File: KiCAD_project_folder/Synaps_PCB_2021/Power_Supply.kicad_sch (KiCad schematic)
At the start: 35 parts, among them J1 USB_C_Receptacle, Q2 Q_PMOS_DGS, U1 MAX14748BEWW+

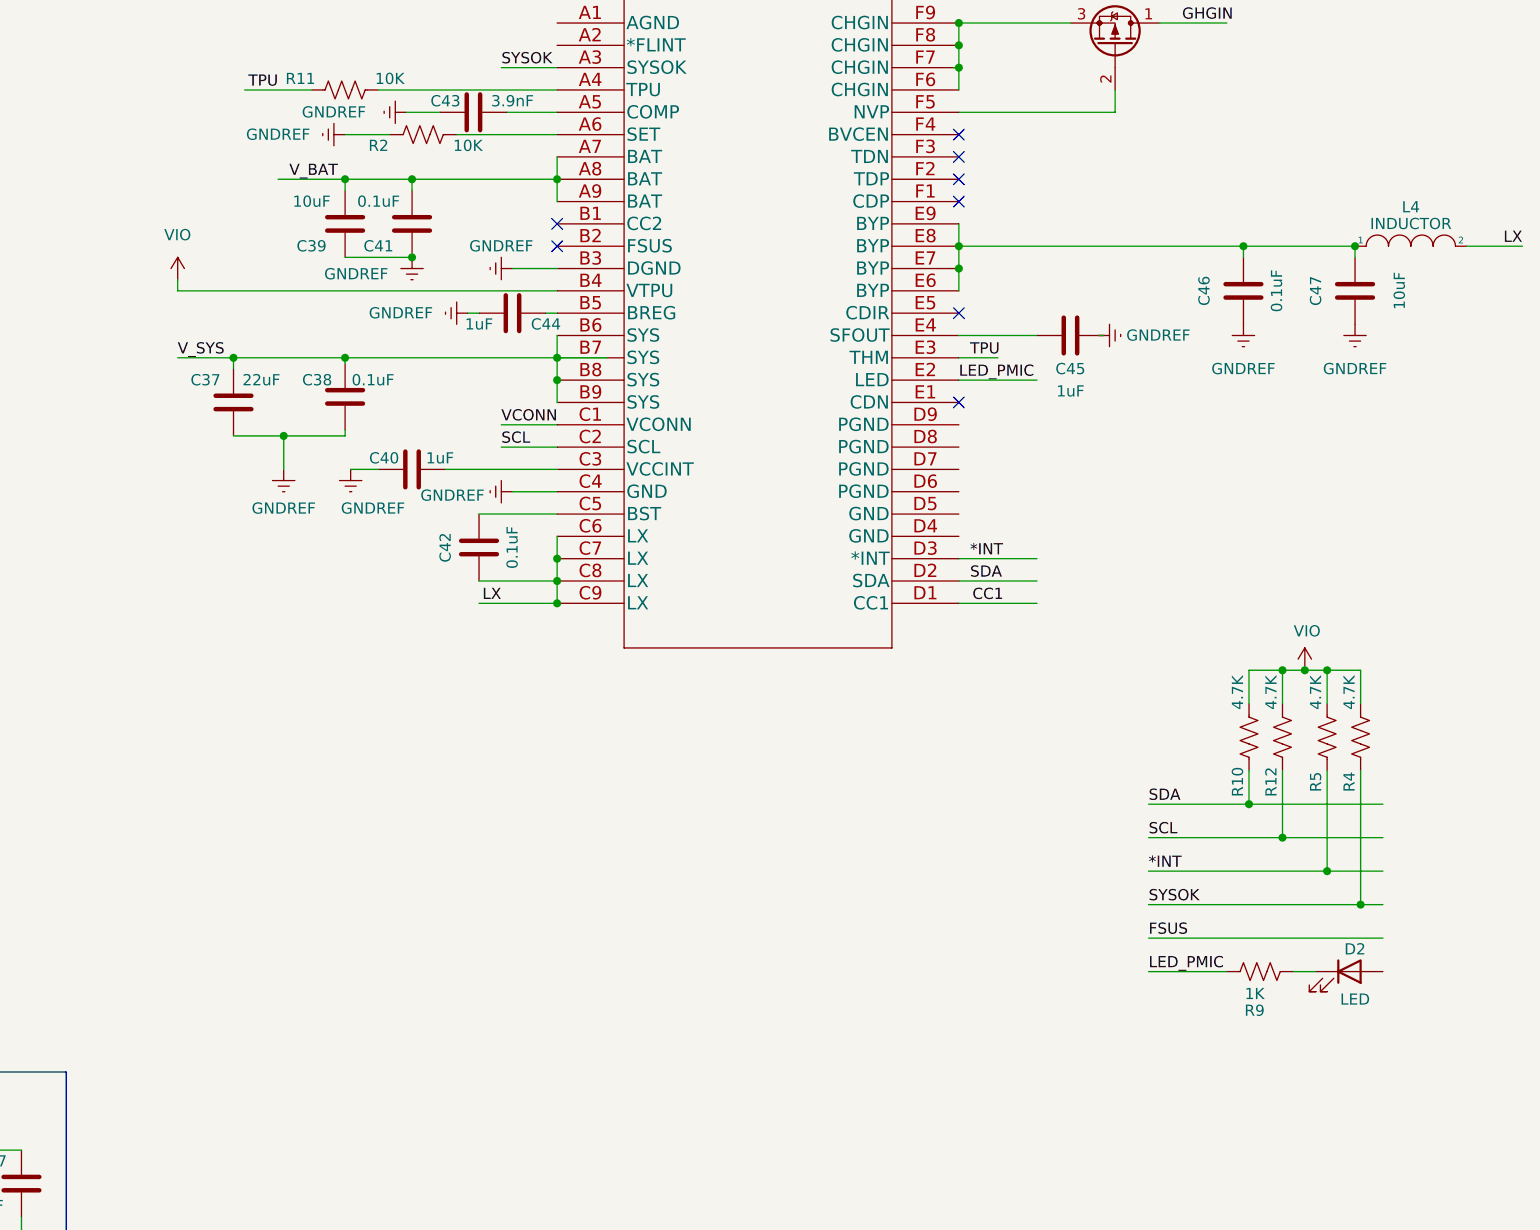
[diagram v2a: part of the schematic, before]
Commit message: Reworded PMIC and probe select
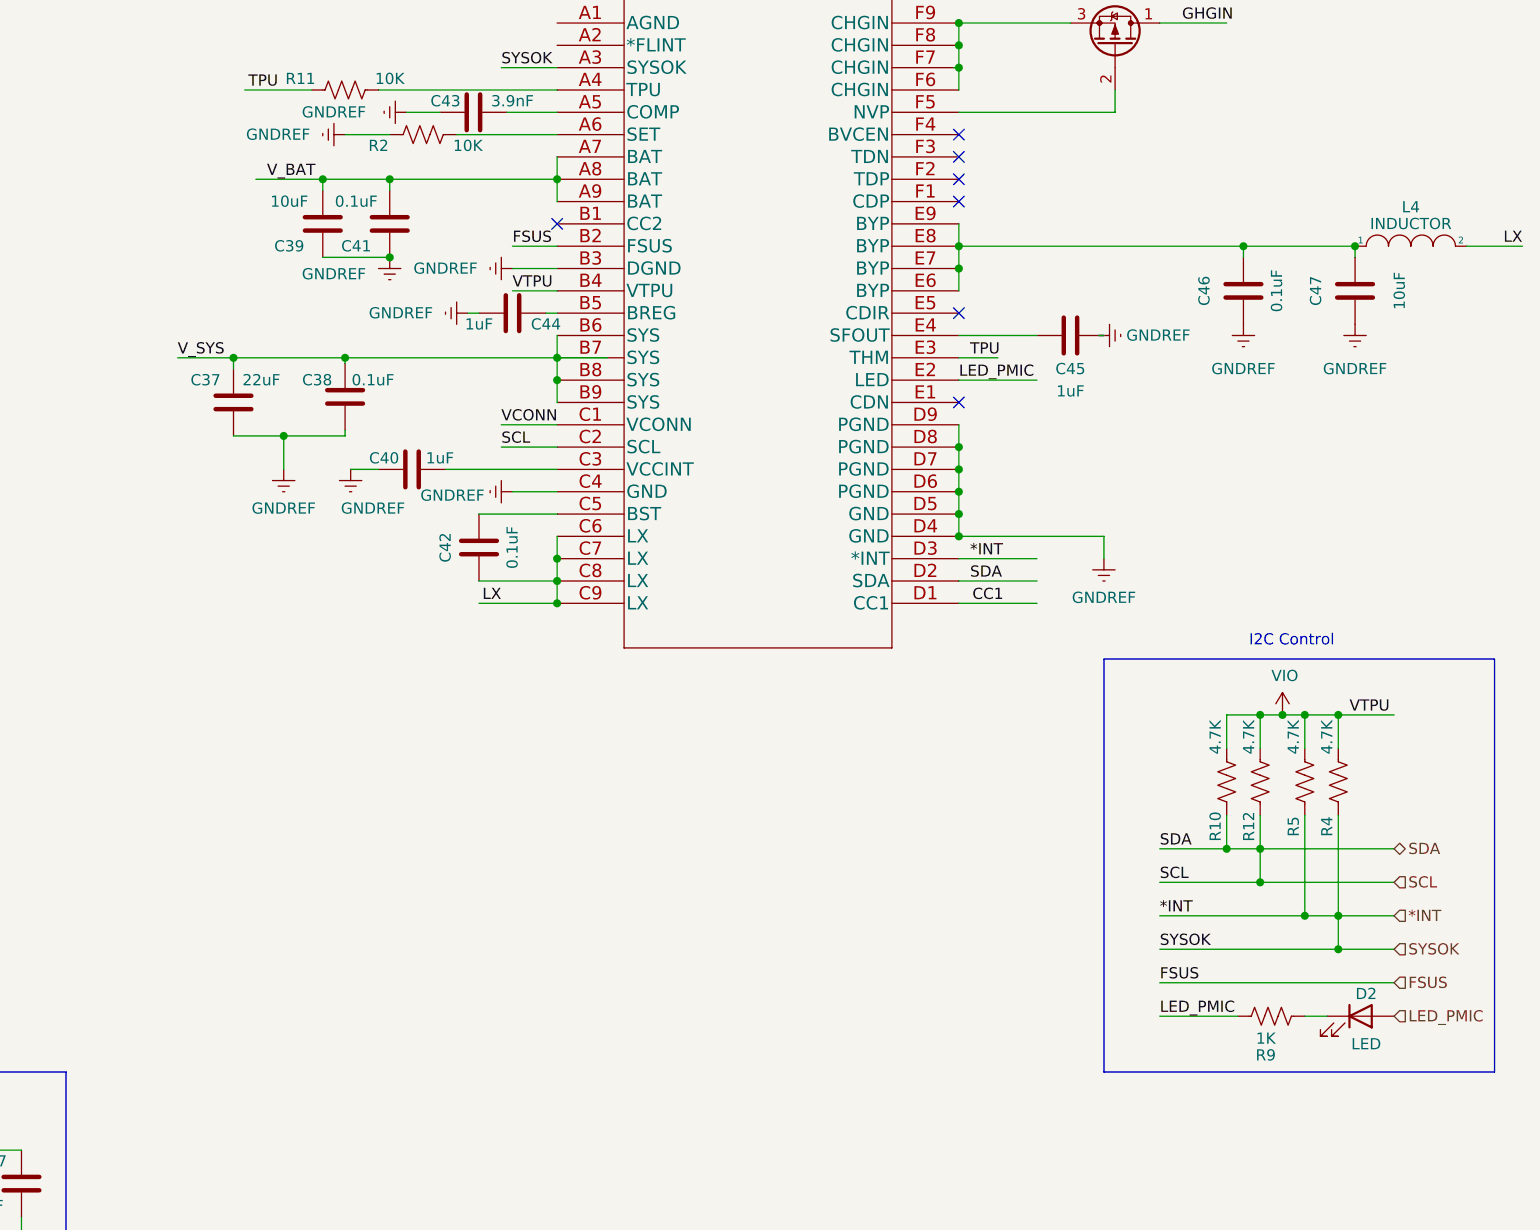
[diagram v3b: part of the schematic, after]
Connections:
- net SDA is gone; now on net SCL: R10.2, U1.D2 (SDA)
- net SYSOK is gone; now on net *INT: R4.1, U1.A3 (SYSOK)
- net FSUS: now also U1.B2 (FSUS)
- net GNDREF: now also U1.D4 (GND), U1.D5 (GND), U1.D6 (PGND), U1.D7 (PGND), U1.D8 (PGND), U1.D9 (PGND)
- net LED_PMIC: now also D2.2 (A)
- no-connect marks 16 -> 15
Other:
- note added: "I2C Control"
- moved on the sheet: C39, C41, D2, R10, R12, R4, R5, R9

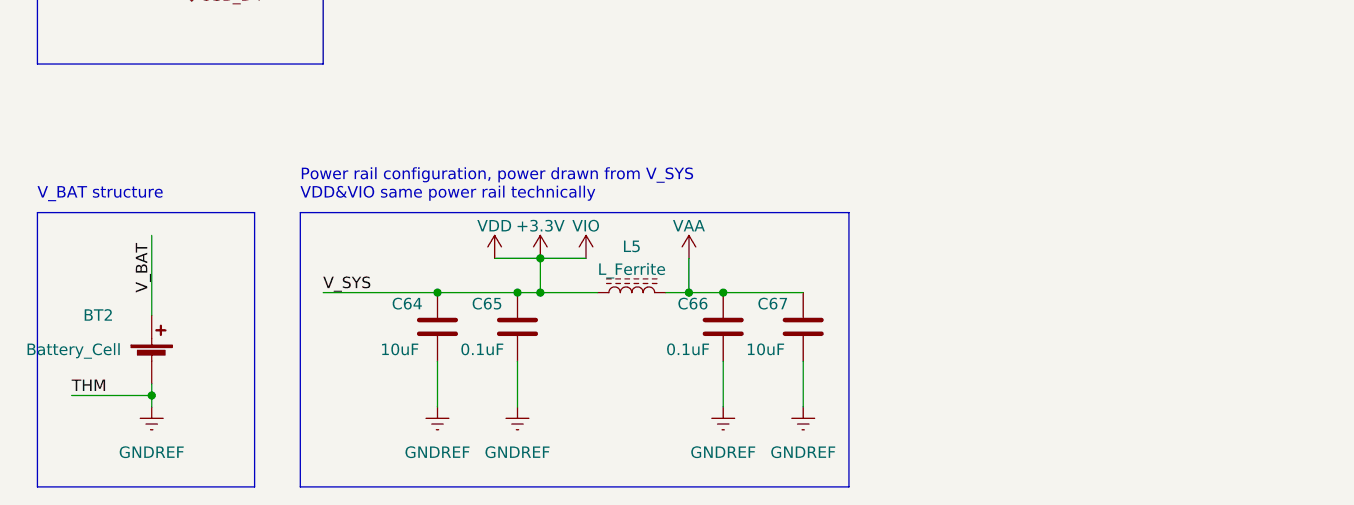
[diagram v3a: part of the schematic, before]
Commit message: Redid schematic, fixed wrong setup
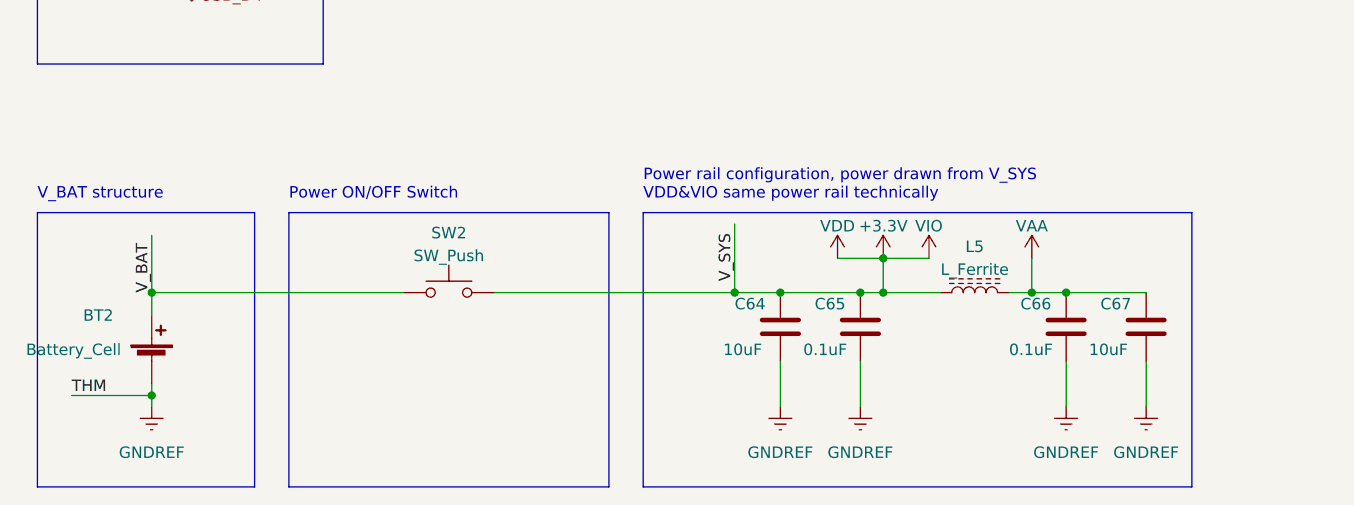
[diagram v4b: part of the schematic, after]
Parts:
- added SW2: SW_Push, symbol Switch:SW_Push
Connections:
- net +1V1: now also SW2.2
- net V_BAT: now also SW2.1
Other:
- note added: "Power ON/OFF Switch"
- moved on the sheet: C64, C65, C66, C67, L5

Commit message: Updated pcb editor with the new components imported
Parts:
- C64, C65, C66, C67: footprint (none) -> Capacitor_SMD:C_1206_3216Metric_Pad1.33x1.80mm_HandSolder
- L5: footprint (none) -> Ferrite_THT:LairdTech_28C0236-0JW-10
- Q2: footprint (none) -> Transformer_NF_ETAL_P2781
- R3: footprint (none) -> Resistor_SMD:R_1206_3216Metric_Pad1.30x1.75mm_HandSolder
- SW2: footprint (none) -> Button_Switch_SMD:SW_Push_1P1T_NO_6x6mm_H9.5mm
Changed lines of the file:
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@@
       (effects (font (size 1.27 1.27)) (justify right))
     )
-    (property "Footprint" "" (id 2) (at 27.686 101.346 90)
+    (property "Footprint" "Resistor_SMD:R_1206_3216Metric_Pad1.30x1.75mm_HandSolder" (id 2) (at 27.686 101.346 90)
       (effects (font (size 1.27 1.27)) hide)
     )
@@
     (property "Reference" "Q2" (id 0) (at 228.6 36.195 90))
     (property "Value" "Q_PMOS_DGS" (id 1) (at 228.6 38.735 90))
-    (property "Footprint" "" (id 2) (at 231.14 40.64 0)
+    (property "Footprint" "Transformer_NF_ETAL_P2781" (id 2) (at 231.14 40.64 0)
       (effects (font (size 1.27 1.27)) hide)
     )
@@
     (property "Reference" "L5" (id 0) (at 123.19 166.3532 90))
     (property "Value" "L_Ferrite" (id 1) (at 123.19 168.8901 90))
-    (property "Footprint" "" (id 2) (at 123.19 171.45 0)
+    (property "Footprint" "Ferrite_THT:LairdTech_28C0236-0JW-10" (id 2) (at 123.19 171.45 0)
       (effects (font (size 1.27 1.27)) hide)
     )
@@
       (effects (font (size 1.27 1.27)) (justify left))
     )
-    (property "Footprint" "" (id 2) (at 134.3152 179.07 0)
+    (property "Footprint" "Capacitor_SMD:C_1206_3216Metric_Pad1.33x1.80mm_HandSolder" (id 2) (at 134.3152 179.07 0)
       (effects (font (size 1.27 1.27)) hide)
     )
@@
       (effects (font (size 1.27 1.27)) (justify left))
     )
-    (property "Footprint" "" (id 2) (at 143.2052 179.07 0)
+    (property "Footprint" "Capacitor_SMD:C_1206_3216Metric_Pad1.33x1.80mm_HandSolder" (id 2) (at 143.2052 179.07 0)
       (effects (font (size 1.27 1.27)) hide)
     )
@@
       (effects (font (size 1.27 1.27)) (justify left))
     )
-    (property "Footprint" "" (id 2) (at 111.4552 179.07 0)
+    (property "Footprint" "Capacitor_SMD:C_1206_3216Metric_Pad1.33x1.80mm_HandSolder" (id 2) (at 111.4552 179.07 0)
       (effects (font (size 1.27 1.27)) hide)
     )
@@
     (property "Reference" "SW2" (id 0) (at 64.77 164.8292 0))
     (property "Value" "SW_Push" (id 1) (at 64.77 167.3661 0))
-    (property "Footprint" "" (id 2) (at 64.77 166.37 0)
+    (property "Footprint" "Button_Switch_SMD:SW_Push_1P1T_NO_6x6mm_H9.5mm" (id 2) (at 64.77 166.37 0)
       (effects (font (size 1.27 1.27)) hide)
     )
@@
       (effects (font (size 1.27 1.27)) (justify left))
     )
-    (property "Footprint" "" (id 2) (at 102.5652 179.07 0)
-      (effects (font (size 1.27 1.27)) hide)
-    )
+    (property "Footprint" "Capacitor_SMD:C_1206_3216Metric_Pad1.33x1.80mm_HandSolder" (id 2) (at 102.5652 179.07 0)
+      (effects (font (size 1.27 1.27)) hide)
+    )

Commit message: Update schematic sheets and creates image to allow the board setup to be shared
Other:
- company: (none) -> Club SynapsÉTS
- title: (none) -> Misca PCB
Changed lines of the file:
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@@
 (kicad_sch (version 20211123) (generator eeschema)
   (paper "A4")
+  (title_block
+    (title "Misca PCB")
+    (date "2022-06-17")
+    (rev "A2")
+    (company "Club SynapsÉTS")
+    (comment 1 "Auteur : Jacques Veneziano")
+  )
   (junction (at 245.11 140.97) (diameter 0) (color 0 0 0 0)
   )
